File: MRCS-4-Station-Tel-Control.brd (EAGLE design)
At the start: 106 x 100 mm, 22 parts, among them CON1 LEDs and Buttons RJ, CON2 LEDS & Pwr RJ, J1 LEDs & Buttons ST, J2 LEDS & Pwr ST

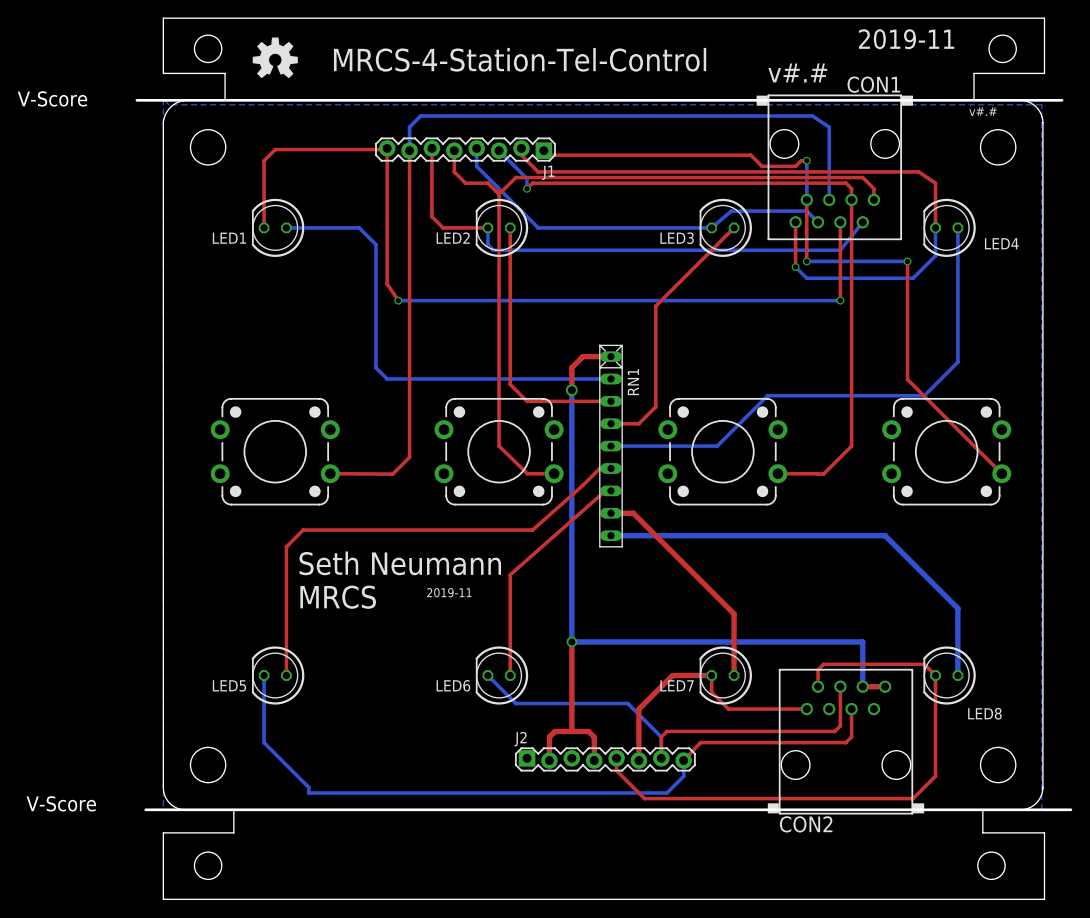
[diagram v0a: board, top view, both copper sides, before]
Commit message: Moved labels for push buttons and LEDs to back
A learning exercise involving mirror, rotate and a lot of moving traces from top to bottom and vice versa
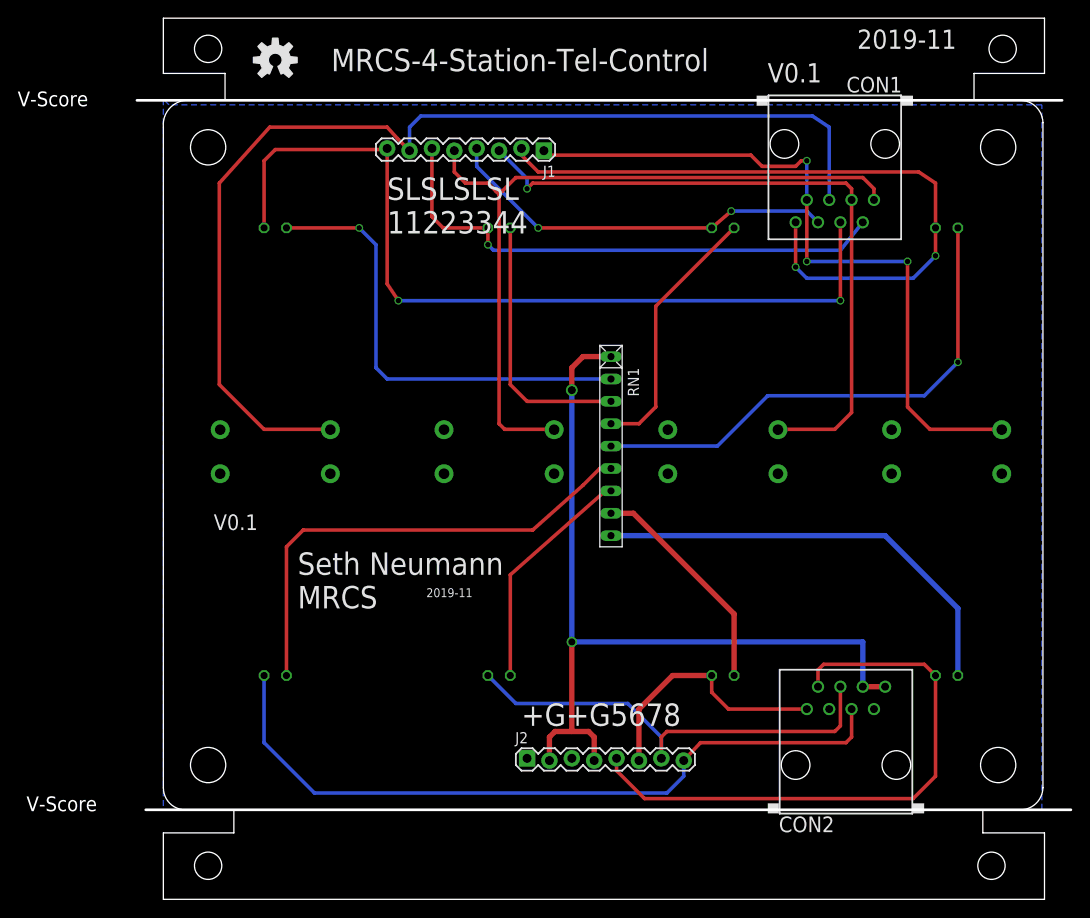
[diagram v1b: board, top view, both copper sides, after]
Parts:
- CON2: value LEDS & Pwr RJ -> Off Hook LEDS & Pwr RJ
- J2: value LEDS & Pwr ST -> Off-Hook LEDS & Pwr ST
- flipped LED1 to the bottom, turned to 180 degrees
- flipped LED2 to the bottom, turned to 180 degrees
- flipped LED3 to the bottom, turned to 180 degrees
- flipped LED4 to the bottom, turned to 180 degrees
- flipped LED5 to the bottom, turned to 180 degrees
- flipped LED6 to the bottom, turned to 180 degrees
- flipped LED7 to the bottom, turned to 180 degrees
- flipped LED8 to the bottom, turned to 180 degrees
- flipped S1 to the bottom, turned to 180 degrees
- flipped S2 to the bottom, turned to 180 degrees
- flipped S3 to the bottom, turned to 180 degrees
- flipped S4 to the bottom, turned to 180 degrees
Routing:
- net N$13: track 104.0 -> 122.6 mm
- net N$14: track 81.9 -> 77.5 mm
- net N$12: track 90.0 -> 86.4 mm
- net N$4: vias 0 -> 1
- net N$18: vias 0 -> 1
- net N$17: vias 1 -> 2
- net N$15: vias 0 -> 2
- net N$1: vias 0 -> 1
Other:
- board text added: "+G+G5678"
- board text added: "SLSLSLSL 11223344"
- board text added: "This side towards fascia"
- board text added: "V0.1"
- board text removed: "v#.#"
